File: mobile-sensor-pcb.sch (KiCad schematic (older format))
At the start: 27 parts, among them U1 NCP551

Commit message: Add more components and footprints
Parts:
- removed C1: 10 uF, Capacitors_SMD:C_1206_HandSoldering, symbol C_Small
- removed C2: C_Small, Capacitors_SMD:C_1206_HandSoldering, symbol C_Small
- removed U1: NCP551, Housings_SOT-23_SOT-143_TSOT-6:SOT-23-5, symbol NCP551
- added U1: 3M_2908-05WB-MG, rascalmicro-kicad-footprints:3M_2908-05WB-MG, symbol 3M_2908-05WB-MG
- added U2: 74HC4050, Housings_SOIC:SOIC-16_3.9x9.9mm_Pitch1.27mm, symbol 74HC4050
- added U3: FGPMMOPA6H, rascalmicro-kicad-footprints:FGPMMOPA6H, symbol FGPMMOPA6H
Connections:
- wire segments 18 -> 12
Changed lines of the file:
@@
 LIBS:contrib
 LIBS:valves
+LIBS:mobile-sensor-pcb-cache
 EELAYER 25 0
 EELAYER END
@@
 $EndDescr
 $Comp
-L NCP551 U1
-U 1 1 55F19AA4
-P 7550 2500
-F 0 "U1" H 7550 2400 50  0000 C CNN
-F 1 "NCP551" H 7550 2600 50  0000 C CNN
-F 2 "Housings_SOT-23_SOT-143_TSOT-6:SOT-23-5" H 7550 2500 50  0001 C CNN
-F 3 "DOCUMENTATION" H 7550 2500 50  0001 C CNN
-	1    7550 2500
-	1    0    0    -1
-$EndComp
-$Comp
-L C_Small C1
-U 1 1 55F19D2D
-P 5950 2550
-F 0 "C1" H 5960 2620 50  0000 L CNN
-F 1 "10 uF" H 5960 2470 50  0000 L CNN
-F 2 "Capacitors_SMD:C_1206_HandSoldering" H 5950 2550 60  0001 C CNN
-F 3 "" H 5950 2550 60  0000 C CNN
-	1    5950 2550
-	1    0    0    -1
-$EndComp
-$Comp
-L C_Small C2
-U 1 1 55F19DA8
-P 8800 2500
-F 0 "C2" H 8810 2570 50  0000 L CNN
-F 1 "C_Small" H 8810 2420 50  0000 L CNN
-F 2 "Capacitors_SMD:C_1206_HandSoldering" H 8800 2500 60  0001 C CNN
-F 3 "" H 8800 2500 60  0000 C CNN
-	1    8800 2500
-	1    0    0    -1
-$EndComp
-Wire Wire Line
-	5950 2400 6800 2400
-Wire Wire Line
-	5950 2700 6350 2700
-Wire Wire Line
-	6350 2700 6350 2500
-Wire Wire Line
-	6350 2500 6800 2500
-Wire Wire Line
-	5950 2700 5950 2650
-Wire Wire Line
-	5950 2400 5950 2450
-$Comp
 L Led_Small LED1
 U 1 1 55F1D029
@@
 	1    0    0    -1
 $EndComp
+$Comp
+L FGPMMOPA6H U3
+U 1 1 55F32348
+P 5800 5000
+F 0 "U3" H 6450 5950 60  0000 C CNN
+F 1 "FGPMMOPA6H" H 6650 5000 60  0000 C CNN
+F 2 "rascalmicro-kicad-footprints:FGPMMOPA6H" H 5800 5000 60  0001 C CNN
+F 3 "" H 5800 5000 60  0000 C CNN
+	1    5800 5000
+	1    0    0    -1
+$EndComp
+$Comp
+L 3M_2908-05WB-MG U1
+U 1 1 55F32015
+P 3950 4500
+F 0 "U1" H 3950 4000 40  0000 C CNN
+F 1 "3M_2908-05WB-MG" H 4000 5050 30  0000 C CNN
+F 2 "rascalmicro-kicad-footprints:3M_2908-05WB-MG" H 3950 4500 60  0001 C CNN
+F 3 "" H 3950 4500 60  0000 C CNN
+	1    3950 4500
+	1    0    0    -1
+$EndComp
+$Comp
+L 74HC4050 U2
+U 1 1 55F321E3
+P 4050 5850
+F 0 "U2" H 3800 6300 60  0000 C CNN
+F 1 "74HC4050" H 3700 6200 60  0000 C CNN
+F 2 "Housings_SOIC:SOIC-16_3.9x9.9mm_Pitch1.27mm" H 4050 5850 60  0001 C CNN
+F 3 "" H 4050 5850 60  0000 C CNN
+	1    4050 5850
+	1    0    0    -1
+$EndComp

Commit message: More components added
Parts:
- added BT?: Battery, symbol Battery
- added C1, C10, C11, C12, C2, C3, C4, C5, C6, C7, C8, C9: 10 uF, symbol C_Small
- added C13: 2.2 uF, symbol C_Small
- added C14, C15, C16: 100 nF, symbol C_Small
- added C17, C18, C19: 10 nF, symbol C_Small
- added C20: 100 uF, symbol C_Small
- added F?: F_Small, symbol F_Small
- added FB1, FB2, FB3, FB4, FB5, FB6, FB7: FILTER, symbol FILTER
- added R13, R14, R15, R16, R17: 10k, symbol R_Small
- added SHIELD?: ARDUINO_DUE_SHIELD, FT:ARDUINO_DUE_SHIELD, symbol ARDUINO_DUE_SHIELD
- added SW1: RESET, symbol SW_PUSH
- added U4: RT9193, symbol RT9193
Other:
- moved on the sheet: LED1, LED10, LED11, LED12, LED2, LED3, LED4, LED5, LED6, LED7, LED8, LED9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

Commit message: More components, plus update footprint library rev
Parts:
- added J1: SMA, rascalmicro_kicad_footprints:SMA, symbol SMA
- added U5: MIC5219, Housings_SOT-23_SOT-143_TSOT-6:SOT-23-5, symbol MIC5219
- added X1: XBEE, freetronics_footprints:XBEE_PRO, symbol XBEE
- C1, C10, C11, C12, C13, C14, C15, C16, C17, C18, C19, C2, C20, C3, C4, C5, C6, C7, C8, C9: footprint (none) -> Capacitors_SMD:C_1206_HandSoldering
- F1: renamed from F?; footprint (none) -> Fuse_Holders_and_Fuses:Fuse_SMD1206_HandSoldering
- FB1, FB2, FB3, FB4, FB5, FB6, FB7, R13, R14, R15, R16, R17: footprint (none) -> Resistors_SMD:R_0805_HandSoldering
- SHIELD1: renamed from SHIELD?; footprint FT:ARDUINO_DUE_SHIELD -> freetronics_footprints:ARDUINO_DUE_SHIELD
- SW1: footprint (none) -> freetronics_footprints:SW_PUSHBUTTON_SMD
- U4: footprint (none) -> Housings_SOT-23_SOT-143_TSOT-6:SOT-23-5
- gave numbers to parts that had none: 1

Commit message: More components, more footprints
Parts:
- added D1: MBR120VLSFT1G, Diodes_SMD:SOD-123, symbol D_Schottky_Small
- added J2: USB_OTG, rascalmicro_kicad_footprints:USB-micro-B-female, symbol USB_OTG
- added J3: JST PH, rascalmicro_kicad_footprints:s2b-ph-sm4-tb, symbol CONN_01X02
- added Q1: PNP-BJT-BIASED_SOT, symbol PNP-BJT-BIASED_SOT
- added SW2: OS102011MA1QS1, rascalmicro_kicad_footprints:OS102011MA1QS1, symbol SWITCH_INV
- added TC1, TC2, TC3: SCREW TERMINAL, freetronics_footprints:SCREWTERMINAL-3.5MM-2, symbol CONN_01X02
- added U10, U11, U12: LP2980AIM5-3.3/NOPB, Housings_SOT-23_SOT-143_TSOT-6:SOT-23-5, symbol RT9193
- added U6: MCP73831T-2ACI/OT, Housings_SOT-23_SOT-143_TSOT-6:SOT-23-5, symbol MCP73831T-2ACI/OT
- added U7, U8, U9: MAX31855KASA, Housings_SOIC:SOIC-8_3.9x4.9mm_Pitch1.27mm, symbol MAX31855KASA
- BT1: footprint (none) -> Discret:CR1220
- F1: value F_Small -> 500 mA fuse
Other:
- moved on the sheet: U2, U4, U5
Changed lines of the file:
@@
 LIBS:valves
 LIBS:freetronics_schematic
+LIBS:transistor
 LIBS:mobile-sensor-pcb-cache
 EELAYER 25 0
@@
 L 74HC4050 U2
 U 1 1 55F321E3
-P 4050 5850
-F 0 "U2" H 3800 6300 60  0000 C CNN
-F 1 "74HC4050" H 3700 6200 60  0000 C CNN
-F 2 "Housings_SOIC:SOIC-16_3.9x9.9mm_Pitch1.27mm" H 4050 5850 60  0001 C CNN
-F 3 "" H 4050 5850 60  0000 C CNN
-	1    4050 5850
+P 3750 5900
+F 0 "U2" H 3500 6350 60  0000 C CNN
+F 1 "74HC4050" H 3400 6250 60  0000 C CNN
+F 2 "Housings_SOIC:SOIC-16_3.9x9.9mm_Pitch1.27mm" H 3750 5900 60  0001 C CNN
+F 3 "" H 3750 5900 60  0000 C CNN
+	1    3750 5900
 	1    0    0    -1
 $EndComp
@@
 P 8800 2750
 F 0 "F1" H 8760 2810 50  0000 L CNN
-F 1 "F_Small" H 8680 2690 50  0000 L CNN
+F 1 "500 mA fuse" H 8680 2690 50  0000 L CNN
 F 2 "Fuse_Holders_and_Fuses:Fuse_SMD1206_HandSoldering" H 8800 2750 60  0001 C CNN
 F 3 "" H 8800 2750 60  0000 C CNN
@@
 F 0 "BT1" H 4350 2650 50  0000 L CNN
 F 1 "Battery" H 4350 2550 50  0000 L CNN
-F 2 "" V 4250 2640 60  0001 C CNN
+F 2 "Discret:CR1220" V 4250 2640 60  0001 C CNN
 F 3 "" V 4250 2640 60  0000 C CNN
 	1    4250 2600
@@
 L RT9193 U4
 U 1 1 55FAE82E
-P 4150 7000
-F 0 "U4" H 4050 7300 60  0000 C CNN
-F 1 "RT9193" H 4150 7200 60  0000 C CNN
-F 2 "Housings_SOT-23_SOT-143_TSOT-6:SOT-23-5" H 4150 7000 60  0001 C CNN
-F 3 "" H 4150 7000 60  0000 C CNN
-	1    4150 7000
+P 3450 7350
+F 0 "U4" H 3350 7650 60  0000 C CNN
+F 1 "RT9193" H 3450 7550 60  0000 C CNN
+F 2 "Housings_SOT-23_SOT-143_TSOT-6:SOT-23-5" H 3450 7350 60  0001 C CNN
+F 3 "" H 3450 7350 60  0000 C CNN
+	1    3450 7350
 	1    0    0    -1
 $EndComp
@@
 L MIC5219 U5
 U 1 1 55FB1D9A
-P 5400 6550
-F 0 "U5" H 5400 6350 60  0000 C CNN
-F 1 "MIC5219" H 5400 6850 60  0000 C CNN
-F 2 "Housings_SOT-23_SOT-143_TSOT-6:SOT-23-5" H 5400 6550 60  0001 C CNN
-F 3 "" H 5400 6550 60  0000 C CNN
-	1    5400 6550
+P 4550 7350
+F 0 "U5" H 4550 7150 60  0000 C CNN
+F 1 "MIC5219" H 4550 7650 60  0000 C CNN
+F 2 "Housings_SOT-23_SOT-143_TSOT-6:SOT-23-5" H 4550 7350 60  0001 C CNN
+F 3 "" H 4550 7350 60  0000 C CNN
+	1    4550 7350
 	1    0    0    -1
 $EndComp
@@
 	1    0    0    -1
 $EndComp
+$Comp
+L USB_OTG J2
+U 1 1 55FC5CC7
+P 2800 950
+F 0 "J2" H 3125 825 50  0000 C CNN
+F 1 "USB_OTG" H 2800 1150 50  0000 C CNN
+F 2 "rascalmicro_kicad_footprints:USB-micro-B-female" V 2750 850 60  0001 C CNN
+F 3 "" V 2750 850 60  0000 C CNN
+	1    2800 950
+	0    -1   -1   0
+$EndComp
+$Comp
+L D_Schottky_Small D1
+U 1 1 55FC64C3
+P 3900 1050
+F 0 "D1" H 3850 1130 50  0000 L CNN
+F 1 "MBR120VLSFT1G" H 3620 970 50  0000 L CNN
+F 2 "Diodes_SMD:SOD-123" V 3900 1050 60  0001 C CNN
+F 3 "" V 3900 1050 60  0000 C CNN
+	1    3900 1050
+	0    1    1    0
+$EndComp
+$Comp
+L MCP73831T-2ACI/OT U6
+U 1 1 55FC8765
+P 7000 5900
+F 0 "U6" H 7000 5575 60  0000 C CNN
+F 1 "MCP73831T-2ACI/OT" H 6950 6250 60  0000 C CNN
+F 2 "Housings_SOT-23_SOT-143_TSOT-6:SOT-23-5" H 7025 5775 60  0001 C CNN
+F 3 "" H 7025 5775 60  0000 C CNN
+	1    7000 5900
+	1    0    0    -1
+$EndComp
+$Comp
+L MAX31855KASA U7
+U 1 1 55FC8B82
+P 10550 4350
+F 0 "U7" H 10200 4750 50  0000 L CNN
+F 1 "MAX31855KASA" H 10650 4750 50  0000 L CNN
+F 2 "Housings_SOIC:SOIC-8_3.9x4.9mm_Pitch1.27mm" H 10550 4350 50  0000 C CIN
+F 3 "" H 10550 4350 60  0000 C CNN
+	1    10550 4350
+	1    0    0    -1
+$EndComp
+$Comp
+L MAX31855KASA U8
+U 1 1 55FC9E74
+P 10350 5400
+F 0 "U8" H 10000 5800 50  0000 L CNN
+F 1 "MAX31855KASA" H 10450 5800 50  0000 L CNN
+F 2 "Housings_SOIC:SOIC-8_3.9x4.9mm_Pitch1.27mm" H 10350 5400 50  0000 C CIN
+F 3 "" H 10350 5400 60  0000 C CNN
+	1    10350 5400
+	1    0    0    -1
+$EndComp
+$Comp
+L MAX31855KASA U9
+U 1 1 55FCA0DA
+P 9600 6350
+F 0 "U9" H 9250 6750 50  0000 L CNN
+F 1 "MAX31855KASA" H 9700 6750 50  0000 L CNN
+F 2 "Housings_SOIC:SOIC-8_3.9x4.9mm_Pitch1.27mm" H 9600 6350 50  0000 C CIN
+F 3 "" H 9600 6350 60  0000 C CNN
+	1    9600 6350
+	1    0    0    -1
+$EndComp
+$Comp
+L CONN_01X02 J3
+U 1 1 55FCAE8B
+P 5500 950
+F 0 "J3" H 5500 1100 50  0000 C CNN
+F 1 "JST PH" V 5600 950 50  0000 C CNN
+F 2 "rascalmicro_kicad_footprints:s2b-ph-sm4-tb" H 5500 950 60  0001 C CNN
+F 3 "" H 5500 950 60  0000 C CNN
+	1    5500 950
+	1    0    0    -1
+$EndComp
+$Comp
+L CONN_01X02 TC1
+U 1 1 55FCC8FD
+P 6300 1000
+F 0 "TC1" H 6300 1150 50  0000 C CNN
+F 1 "SCREW TERMINAL" V 6400 1000 50  0000 C CNN
+F 2 "freetronics_footprints:SCREWTERMINAL-3.5MM-2" H 6300 1000 60  0001 C CNN
+F 3 "" H 6300 1000 60  0000 C CNN
+	1    6300 1000
+	1    0    0    -1
+$EndComp
+$Comp
+L CONN_01X02 TC2
+U 1 1 55FCCB44
+P 6800 1000
+F 0 "TC2" H 6800 1150 50  0000 C CNN
+F 1 "SCREW TERMINAL" V 6900 1000 50  0000 C CNN
+F 2 "freetronics_footprints:SCREWTERMINAL-3.5MM-2" H 6800 1000 60  0001 C CNN
+F 3 "" H 6800 1000 60  0000 C CNN
+	1    6800 1000
+	1    0    0    -1
+$EndComp
+$Comp
+L CONN_01X02 TC3
+U 1 1 55FCCC3C
+P 7150 1000
+F 0 "TC3" H 7150 1150 50  0000 C CNN
+F 1 "SCREW TERMINAL" V 7250 1000 50  0000 C CNN
+F 2 "freetronics_footprints:SCREWTERMINAL-3.5MM-2" H 7150 1000 60  0001 C CNN
+F 3 "" H 7150 1000 60  0000 C CNN
+	1    7150 1000
+	1    0    0    -1
+$EndComp
+$Comp
+L RT9193 U10
+U 1 1 55FC7FBB
+P 4850 6000
+F 0 "U10" H 4750 6300 60  0000 C CNN
+F 1 "LP2980AIM5-3.3/NOPB" H 4850 6200 60  0000 C CNN
+F 2 "Housings_SOT-23_SOT-143_TSOT-6:SOT-23-5" H 4850 6000 60  0001 C CNN
+F 3 "" H 4850 6000 60  0000 C CNN
+	1    4850 6000
+	1    0    0    -1
+$EndComp
+$Comp
+L SWITCH_INV SW2
+U 1 1 55FC84F8
+P 1500 1150
+F 0 "SW2" H 1300 1300 50  0000 C CNN
+F 1 "OS102011MA1QS1" H 1350 1000 50  0000 C CNN
+F 2 "rascalmicro_kicad_footprints:OS102011MA1QS1" H 1500 1150 60  0001 C CNN
+F 3 "" H 1500 1150 60  0000 C CNN
+	1    1500 1150
+	-1   0    0    -1
+$EndComp
+$Comp
+L RT9193 U11
+U 1 1 55FC8AA4
+P 5700 6750
+F 0 "U11" H 5600 7050 60  0000 C CNN
+F 1 "LP2980AIM5-3.3/NOPB" H 5700 6950 60  0000 C CNN
+F 2 "Housings_SOT-23_SOT-143_TSOT-6:SOT-23-5" H 5700 6750 60  0001 C CNN
+F 3 "" H 5700 6750 60  0000 C CNN
+	1    5700 6750
+	1    0    0    -1
+$EndComp
+$Comp
+L RT9193 U12
+U 1 1 55FC8BAE
+P 6300 7350
+F 0 "U12" H 6200 7650 60  0000 C CNN
+F 1 "LP2980AIM5-3.3/NOPB" H 6300 7550 60  0000 C CNN
+F 2 "Housings_SOT-23_SOT-143_TSOT-6:SOT-23-5" H 6300 7350 60  0001 C CNN
+F 3 "" H 6300 7350 60  0000 C CNN
+	1    6300 7350
+	1    0    0    -1
+$EndComp
+$Comp
+L PNP-BJT-BIASED_SOT Q1
+U 1 1 55FC9720
+P 4750 5150
+F 0 "Q1" H 4700 5300 60  0000 C CNN
+F 1 "PNP-BJT-BIASED_SOT" H 4750 5000 60  0000 C CNN
+F 2 "" H 4750 5150 60  0001 C CNN
+F 3 "" H 4750 5150 60  0001 C CNN
+	1    4750 5150
+	1    0    0    1
+$EndComp
 $EndSCHEMATC

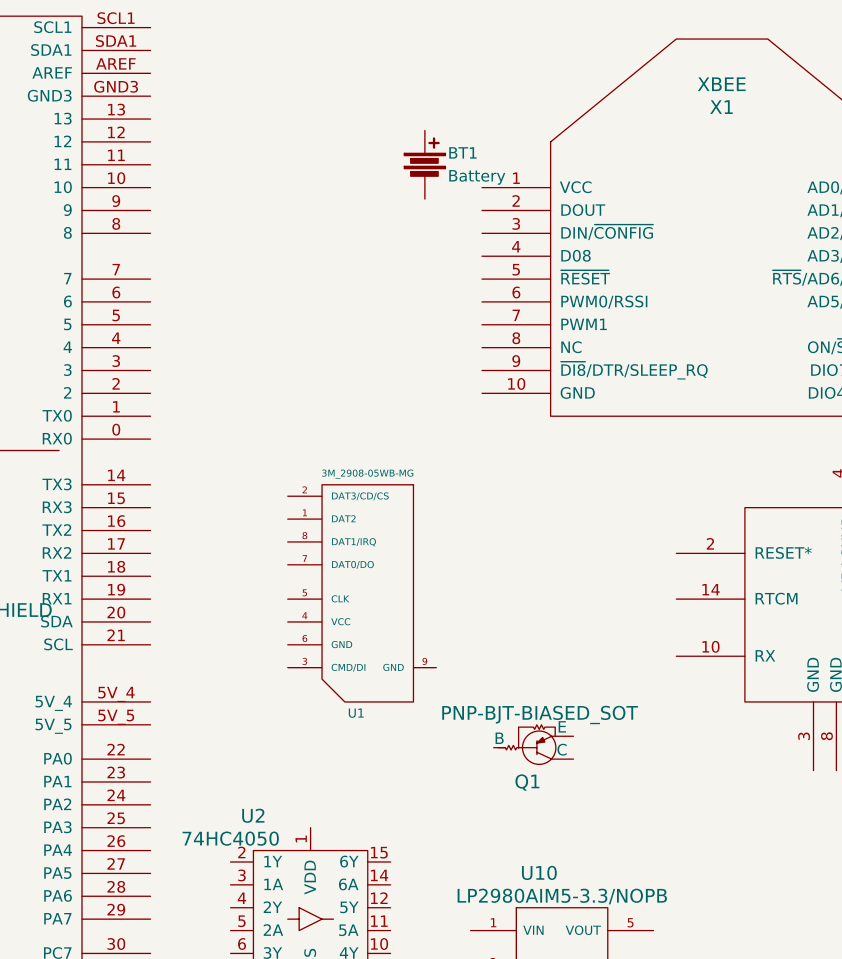
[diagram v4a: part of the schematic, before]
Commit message: First commit with all footprints added
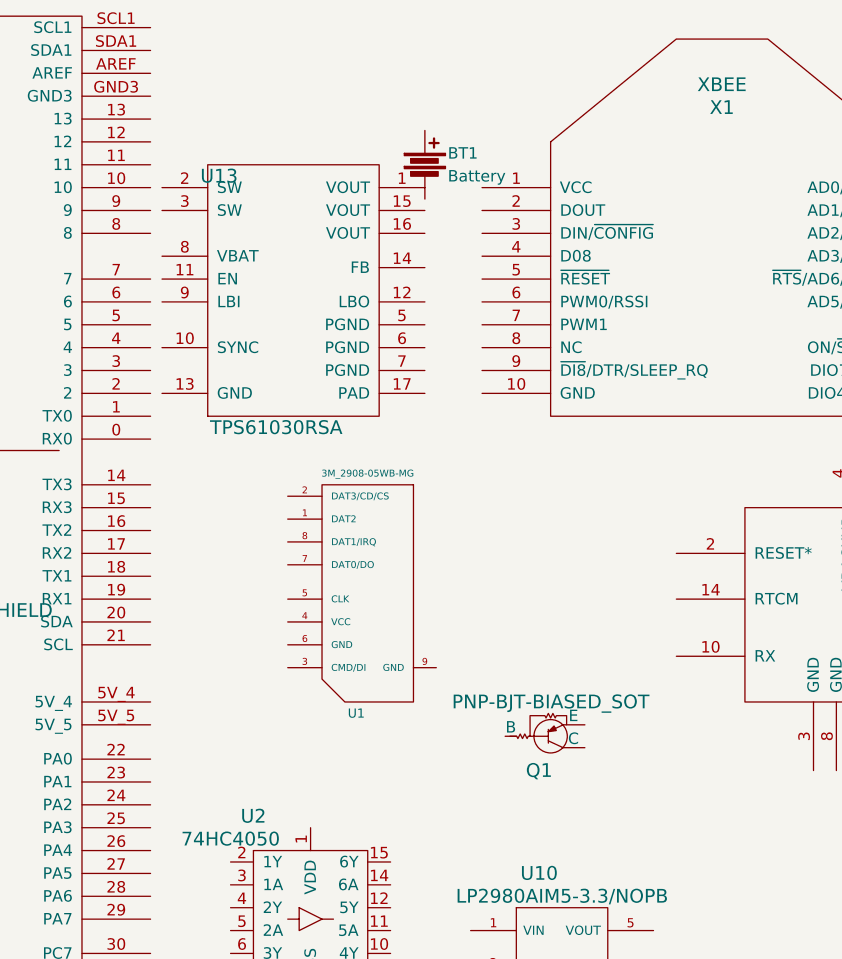
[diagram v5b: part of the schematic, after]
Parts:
- added U13: TPS61030RSA, Housings_DFN_QFN:QFN-16-1EP_4x4mm_Pitch0.65mm, symbol TPS61030RSA
- Q1: footprint (none) -> Housings_SOT-23_SOT-143_TSOT-6:SOT-23_Handsoldering
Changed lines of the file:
@@
 EESchema Schematic File Version 2
+LIBS:mobile-sensor-pcb-rescue
 LIBS:rascalmicro-kicad-library
 LIBS:power
@@
 LIBS:valves
 LIBS:freetronics_schematic
-LIBS:transistor
 LIBS:mobile-sensor-pcb-cache
 EELAYER 25 0
@@
 $Comp
 L PNP-BJT-BIASED_SOT Q1
-U 1 1 55FC9720
-P 4750 5150
-F 0 "Q1" H 4700 5300 60  0000 C CNN
-F 1 "PNP-BJT-BIASED_SOT" H 4750 5000 60  0000 C CNN
-F 2 "" H 4750 5150 60  0001 C CNN
-F 3 "" H 4750 5150 60  0001 C CNN
-	1    4750 5150
+U 1 1 56002B1C
+P 4800 5100
+F 0 "Q1" H 4750 5250 60  0000 C CNN
+F 1 "PNP-BJT-BIASED_SOT" H 4800 4950 60  0000 C CNN
+F 2 "Housings_SOT-23_SOT-143_TSOT-6:SOT-23_Handsoldering" H 4800 5100 60  0001 C CNN
+F 3 "" H 4800 5100 60  0001 C CNN
+	1    4800 5100
 	1    0    0    1
 $EndComp
+$Comp
+L TPS61030RSA U13
+U 1 1 5600564C
+P 3300 3700
+F 0 "U13" H 3350 4750 60  0000 C CNN
+F 1 "TPS61030RSA" H 3600 3650 60  0000 C CNN
+F 2 "Housings_DFN_QFN:QFN-16-1EP_4x4mm_Pitch0.65mm" H 3300 3700 60  0001 C CNN
+F 3 "" H 3300 3700 60  0000 C CNN
+	1    3300 3700
+	1    0    0    -1
+$EndComp
 $EndSCHEMATC

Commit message: Start connecting stuff. Still need a few more resistors.
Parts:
- added R18, R19: 10k, Resistors_SMD:R_0805_HandSoldering, symbol R_Small
- LED1: value RED: XBEE DOUT -> RX
- LED10: value YELLOW: SD CARD DATA -> LOG
- LED11: value GREEN: GPS 3.3 V -> PWR
- LED12: value RED: GPS FIX -> FIX
- LED2: value GREEN: XBEE DIN -> TX
- LED3: value GREEN: XBEE SIGNAL STRENGTH -> SIG
- LED4: value RED: XBEE 3.3 V -> PWR
- LED5: value GREEN: XBEE CONNECTED -> CONN
- LED6: value BLUE: 5 V -> 5V
- LED7: value GREEN: BATTERY FULL -> FULL
- LED8: value YELLOW: BATTERY CHARGING -> CHG
- LED9: value RED: BATTERY DYING -> DEAD
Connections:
- net GND: now also BT1.2, C1.2, C10.2, C13.2, C14.2, C16.2, C2.2, C20.2, C9.2, J1.2 (GND1), J1.5 (GND4), U1.6 (GND), U1.9 (GND), U13.17 (PAD), U13.5 (PGND), U2.8 (VSS), U3.19 (GND), U3.3 (GND), U4.2 (GND), U5.2 (GND), X1.10 (GND)
- net XBEE-3V3: now reaches LED1.2 (A)
- net XBEE-3V3: now also LED2.2 (A), LED4.2 (A), U5.5 (OUT), X1.1 (VCC)
- net XBEE-RSSI: now reaches LED3.2 (A)
- net XBEE-RSSI: now also X1.6 (PWM0/RSSI)
- net XBEE-DIO5: now reaches LED5.2 (A)
- net XBEE-DIO5: now also X1.15 (AD5/DIO5)
- net BATT-5V: now reaches LED6.2 (A)
- net BATT-5V: now also C9.1, D1.1 (K), Q1.2 (E), U4.1 (VIN), U4.3 (EN), U5.1 (IN), U5.3 (EN)
- net BATT-STAT: now reaches LED7.2 (A)
- net BATT-STAT: now also R8.2
- net USB-5V: now reaches LED8.2 (A)
- net BATT-DEAD: now reaches LED9.2 (A)
- net BATT-DEAD: now also Q1.3 (C)
- net SD-CLK: now reaches LED10.2 (A)
- net GPS-SD-3V3: now reaches LED11.2 (A)
- net GPS-SD-3V3: now also C10.1, FB7.1, U1.4 (VCC), U2.1 (VDD), U4.5 (VOUT)
- net GPS-FIX: now reaches LED12.2 (A)
- net GPS-FIX: now also U3.5 (3DFIX)
- net XBEE-DOUT: now reaches R1.2
- net XBEE-DOUT: now also X1.2 (DOUT)
- net XBEE-DIN: now reaches R2.2
- net XBEE-DIN: now also X1.3 (DIN/~CONFIG)
- net at U1.2 (DAT3/CD/CS): now also U2.6 (3Y)
- net at U1.3 (CMD/DI): now also U2.4 (2Y)
- net at U1.5 (CLK): now also U2.2 (1Y)
- net DUE-5V-RX: now reaches U2.11 (5A)
- net DUE-5V-RX: now also SHIELD1.0 (RX0)
- net GPS-3V3-RX: now reaches U2.12 (5Y)
- net GPS-3V3-RX: now also U3.10 (RX)
- net DUE-SCK: now reaches U2.3 (1A)
- net DUE-MOSI: now reaches U2.5 (2A)
- net at U2.7 (3A): now also R19.2
- net at U3.1 (VCC): now also FB7.2
- net at U3.11 (EX_ANT): now also J1.1 (RF)
- net at U3.4 (VBACKUP): now also BT1.1
- net DUE-TX: now reaches U3.9 (TX)
- net DUE-TX: now also SHIELD1.1 (TX0)
- net at C13.1: now also C20.1, F1.2, U13.1 (VOUT), U13.16 (VOUT)
- net RESET: now reaches C15.1
- net RESET: now also X1.4 (D08)
- net at C15.2: now also X1.17 (AD3/DIO3)
- net at F1.1: now also D1.2 (A)
- no-connect marks 0 -> 23
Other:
- moved on the sheet: BT1, C1, C10, C11, C12, C13, C14, C15, C16, C17, C18, C19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

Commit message: Schematic done
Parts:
- removed SW2: OS102011MA1QS1, rascalmicro_kicad_footprints:OS102011MA1QS1, symbol SWITCH_INV
- added C13: 100nF, Capacitors_SMD:C_1206_HandSoldering, symbol C_Small
- added L1: 6.8uH, Inductors_NEOSID:Neosid_Inductor_SM-NE56_SMD2220, symbol INDUCTOR_SMALL
- added R20, R21: 340k, Resistors_SMD:R_0805_HandSoldering, symbol R_Small
- added R22: 200k, Resistors_SMD:R_0805_HandSoldering, symbol R_Small
- added R23, R24: 1.80M, Resistors_SMD:R_0805_HandSoldering, symbol R_Small
- added R25: 2k, Resistors_SMD:R_0805_HandSoldering, symbol R_Small
- added SW2: ON/OFF, freetronics_footprints:SCREWTERMINAL-3.5MM-2, symbol SPST
- renumbered C13 to C21
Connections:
- net DUE-MOSI is gone; now on net SD-MOSI: U2.5 (2A)
- net DUE-SCK is gone; now on net SD-SCK: U2.3 (1A)
- net XBEE-DIN is gone; now on net XBEE-TX: R2.2, X1.3 (DIN/~CONFIG)
- net XBEE-DOUT is gone; now on net XBEE-RX: R1.2, X1.2 (DOUT)
- net BATT-5V: now also SHIELD1.5V, SHIELD1.5V_4, SHIELD1.5V_5, U10.1 (VIN), U10.3 (EN), U11.1 (VIN), U11.3 (EN)
- net BATT-STAT: now also U6.1 (STAT)
- net GND: now also C11.2, C12.2, C3.2, C4.2, C5.2, C6.2, C7.2, C8.2, J2.5 (GND), J3.2 (P2), SHIELD1.GND1, SHIELD1.GND2, SHIELD1.GND3, SHIELD1.GND4, SHIELD1.GND5, SHIELD1.SP6 (Gnd), SW1.2, U10.2 (GND), U11.2 (GND), U12.2 (GND), U13.10 (SYNC), U13.13 (GND), U6.2 (VSS), U7.1 (GND), U8.1 (GND), U9.1 (GND), C13.2, R20.2, R22.2, R25.2, SW2.1
- net USB-5V: now also C12.1, J2.1 (VCC), U6.4 (VDD)
- net SD-MISO: now reaches U1.7 (DAT0/DO)
- net SD-MISO: now also SHIELD1.48 (PL1)
- net SD-CS: now reaches R19.2, U2.7 (3A)
- net SD-CS: now also SHIELD1.44 (PL5)
- net TC-CS0: now reaches SHIELD1.10
- net TC-CS0: now also R14.2, U7.6 (~CS~)
- net XBEE-TX: now reaches SHIELD1.16 (TX2)
- net XBEE-RX: now reaches SHIELD1.17 (RX2)
- net GPS-TX: now reaches SHIELD1.18 (TX1)
- net GPS-TX: now also U3.9 (TX)
- net GPS-5V-RX: now reaches SHIELD1.19 (RX1)
- net GPS-5V-RX: now also U2.11 (5A)
- net TC-CS1: now reaches SHIELD1.4
- net TC-CS1: now also R16.2, U8.6 (~CS~)
- net SD-MOSI: now reaches SHIELD1.46 (PL3)
- net SD-SCK: now reaches SHIELD1.50 (PB3)
- net TC-CS2: now reaches SHIELD1.52 (PB1)
- net TC-CS2: now also R18.2, U9.6 (~CS~)
- net XBEE-RESET: now reaches SHIELD1.RST
- net XBEE-RESET: now also C15.1, SW1.1
- net TC-MISO: now reaches SHIELD1.SP1 (MISO)
- net TC-MISO: now also U7.7 (SO), U8.7 (SO), U9.7 (SO)
- net TC-SCK: now reaches SHIELD1.SP3 (SCK)
- net TC-SCK: now also R13.2, R15.2, R17.2, U7.5 (SCK), U8.5 (SCK), U9.5 (SCK)
- net at C3.1: now also C4.1, R14.1, U10.5 (VOUT), U7.4 (VCC)
- net at C5.1: now also C6.1, R16.1, U11.5 (VOUT), U8.4 (VCC)
- net at C7.1: now also C8.1, R18.1, U12.5 (VOUT), U9.4 (VCC)
- net at C11.1: now also J3.1 (P1), U13.8 (VBAT), U6.3 (VBAT), C13.1, L1.1, R21.2
- net at C17.1: now also FB1.2, U7.3 (T+)
- net at C17.2: now also FB2.2, U7.2 (T-)
- net at C18.1: now also FB3.2, U8.3 (T+)
- net at C18.2: now also FB4.2, U8.2 (T-)
- net at C19.1: now also FB5.2, U9.3 (T+)
- net at C19.2: now also FB6.2, U9.2 (T-)
- net at FB1.1: now also TC1.2 (P2)
- net at FB2.1: now also TC1.1 (P1)
- net at FB3.1: now also TC2.2 (P2)
- net at FB4.1: now also TC2.1 (P1)
- net at FB5.1: now also TC3.2 (P2)
- net at FB6.1: now also TC3.1 (P1)
- net at U6.5 (PROG): now also R25.1
- net at U12.1 (VIN): now also U12.3 (EN)
- net at U13.11 (EN): now also R21.1, SW2.2
- net at U13.14 (FB): now also R22.1, R23.2
- net at U13.2 (SW): now also U13.3 (SW), L1.2
- net at U13.9 (LBI): now also R20.1, R24.2
- net DUE-5V-RX: no longer names the net of SHIELD1.0 (RX0)
- net DUE-5V-RX: no longer U2.11 (5A)
- net DUE-TX: no longer names the net of SHIELD1.1 (TX0)
- net DUE-TX: no longer U3.9 (TX)
- net RESET: no longer names the net of X1.4 (D08)
- net RESET: no longer C15.1
- no-connect marks 23 -> 94
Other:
- moved on the sheet: C11, C12, C17, C18, C19, C3, C4, C5, C6, C7, C8, FB1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
